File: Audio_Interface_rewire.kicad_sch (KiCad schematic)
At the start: 56 parts

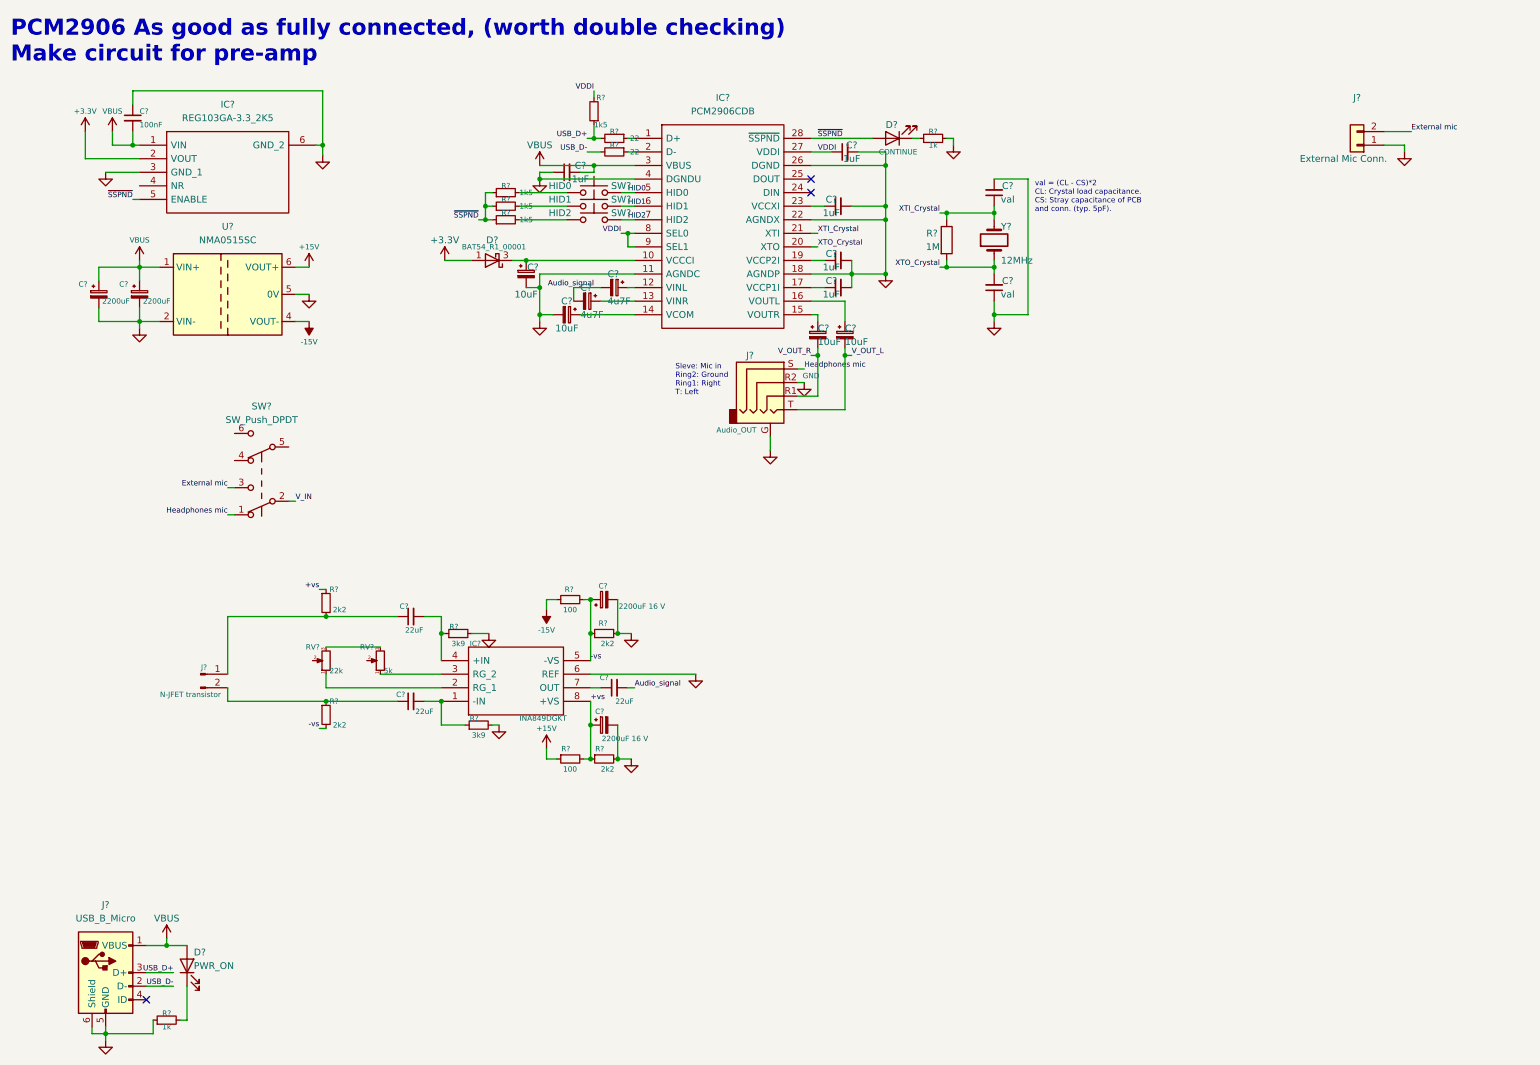
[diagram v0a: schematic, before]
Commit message: First draft of schematic completed
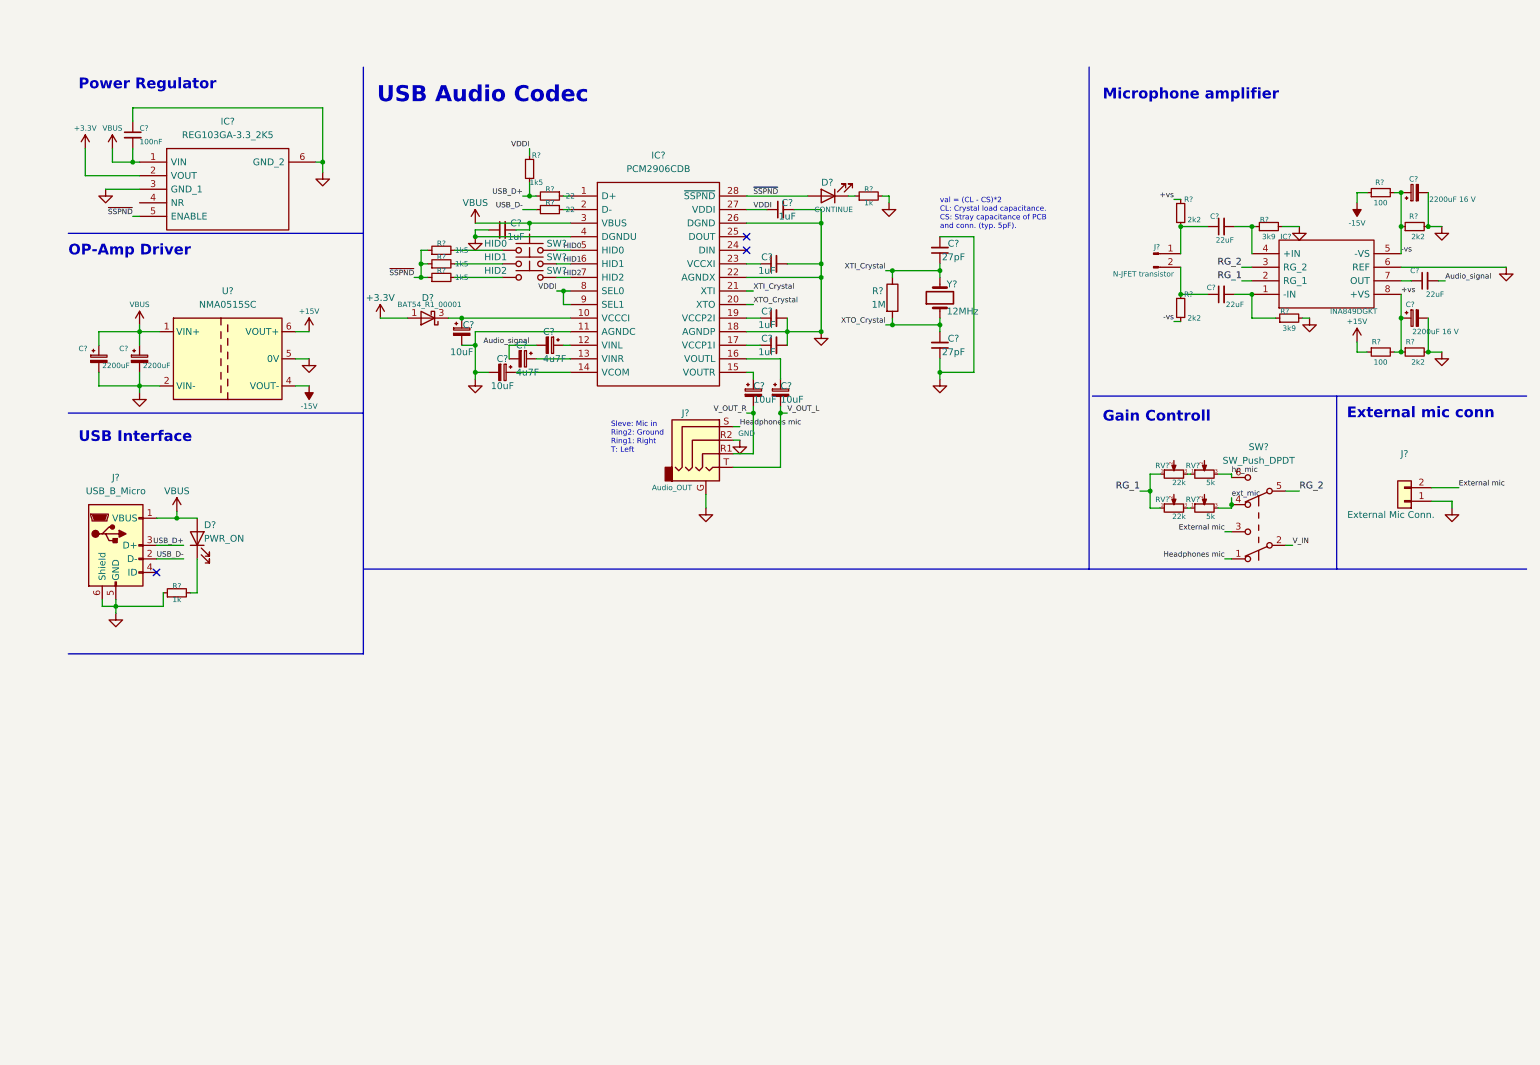
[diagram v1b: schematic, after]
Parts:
- removed RV?: 22k, symbol Device:R_Potentiometer_Small
- removed RV?: 5k, symbol Device:R_Potentiometer_Small
- added RV? (x2): 5k, symbol Device:R_Potentiometer_Small
- added RV? (x2): 22k, symbol Device:R_Potentiometer_Small
- C? (x2): value val -> 27pF
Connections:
- net ext_mic: now reaches SW?.4 (A)
- net ext_mic: now also RV?.3
- net RG_2: now reaches SW?.5 (B)
- net RG_2: now also IC?.3 (RG_2)
- net hp_mic: now reaches SW?.6 (C)
- net hp_mic: now also RV?.3
- net RG_1: now reaches IC?.2 (RG_1)
- net RG_1: now also RV?.1, RV?.1
- new net: RV?.1, RV?.3 (x2)
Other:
- note added: "External mic conn"
- note added: "Gain Controll"
- note added: "Microphone amplifier"
- note added: "OP-Amp Driver"
- note added: "Power Regulator"
- note added: "USB Audio Codec"
- note added: "USB Interface"
- note removed: "PCM2906 As good as fully connected, (worth double checking) Make circuit for pre-amp"
- moved on the sheet: C?, D?, IC?, J?, R?, SW?, U?, Y?

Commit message: Started assigning footprints for pcb, about 1/2 completed
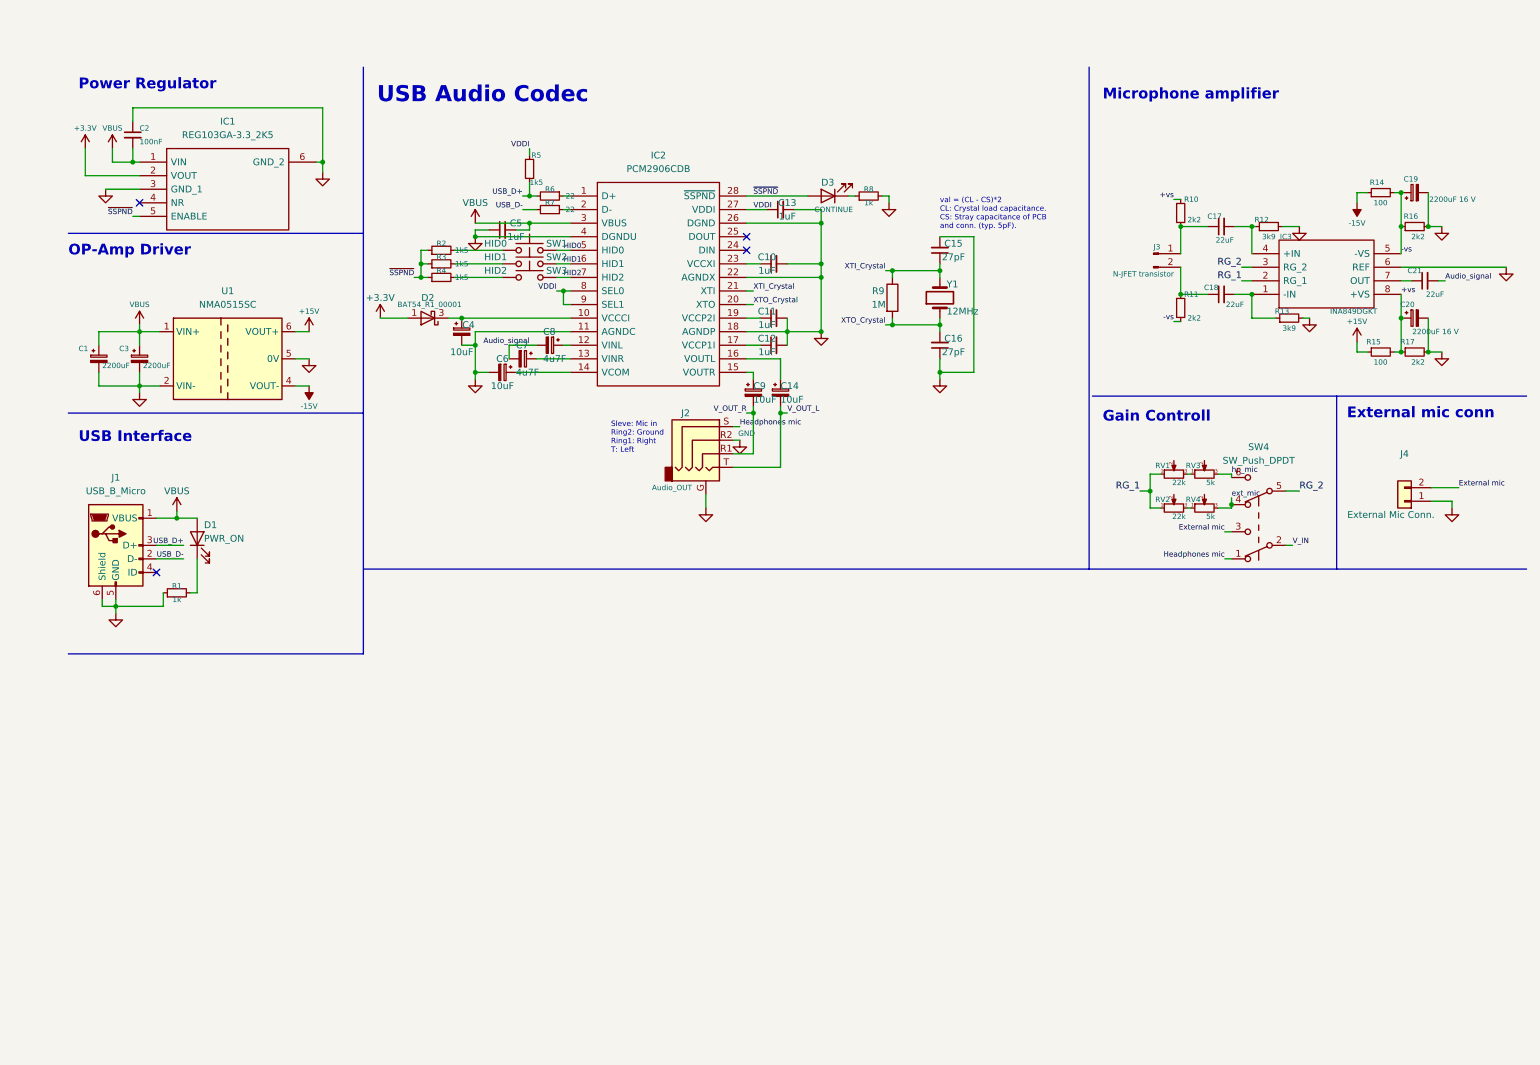
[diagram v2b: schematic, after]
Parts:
- C1, C10, C11, C12, C13, C15, C16, C2, C3, C5: renamed from C?; footprint (none) -> Capacitor_SMD:C_0805_2012Metric_Pad1.18x1.45mm_HandSolder
- C14, C17, C18, C21, C4, C6, C7, C8, C9: renamed from C?; footprint (none) -> Capacitor_THT:CP_Radial_D8.0mm_P5.00mm
- C19, C20: renamed from C?; footprint (none) -> Capacitor_THT:CP_Radial_D12.5mm_P5.00mm
- D1, D3: renamed from D?; footprint (none) -> Diode_SMD:D_0805_2012Metric_Pad1.15x1.40mm_HandSolder
- IC1: renamed from IC?; footprint SOT127P706X180-6N -> IC_Downloaded:SOT127P706X180-6N
- IC2: renamed from IC?; footprint SOP65P780X200-28N -> Package_SO:SOP65P780X200-28N
- IC3: renamed from IC?; footprint SOP65P490X110-8N -> IC_Downloaded:SOP65P490X110-8N
- J1: renamed from J?; footprint (none) -> Connector_USB:USB_B_Lumberg_2411_02_Horizontal
- J2: renamed from J?; footprint (none) -> Connector_Audio:Jack_3.5mm_CUI_SJ1-3535NG_Horizontal
- J3: renamed from J?; footprint (none) -> Package_TO_SOT_SMD:SOT-23
- J4: renamed from J?; footprint (none) -> Connector_JST:JST_XH_B2B-XH-AM_1x02_P2.50mm_Vertical
- gave numbers to parts that had none: 28
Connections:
- no-connect marks 3 -> 4

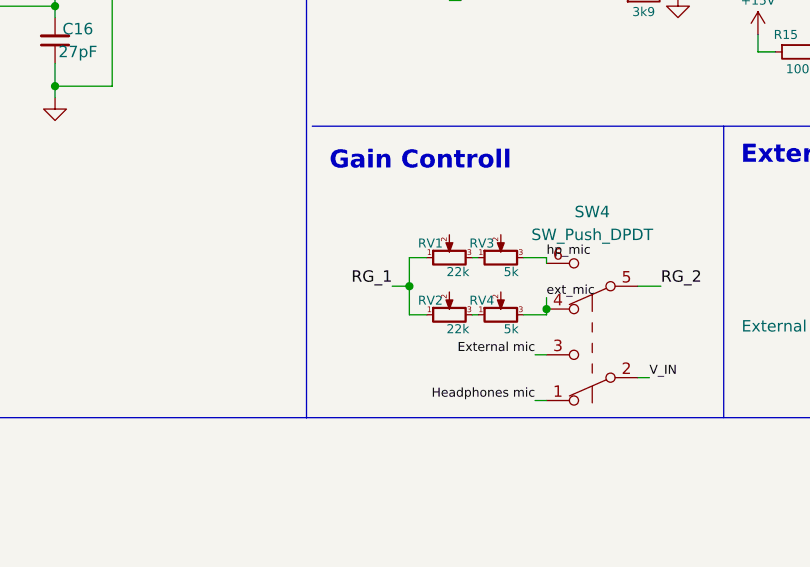
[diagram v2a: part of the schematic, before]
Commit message: Fixed gain control and added resistor footprints
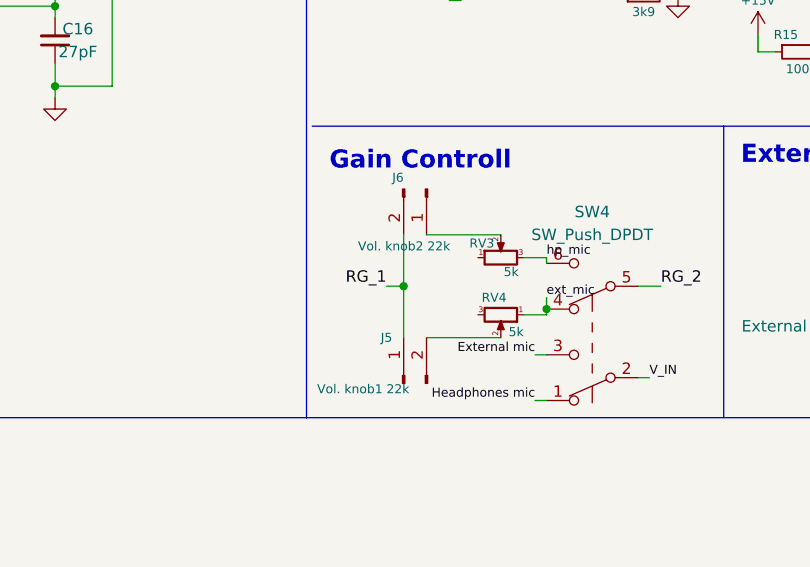
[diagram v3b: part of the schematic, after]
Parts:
- removed RV1, RV2: 22k, symbol Device:R_Potentiometer_Small
- added J5: Vol. knob1 22k, Connector_JST:JST_XH_B2B-XH-AM_1x02_P2.50mm_Vertical, symbol Connector:Conn_01x02_Male
- added J6: Vol. knob2 22k, Connector_JST:JST_XH_B2B-XH-AM_1x02_P2.50mm_Vertical, symbol Connector:Conn_01x02_Male
- R1, R10, R11, R12, R13, R14, R15, R16, R17, R2, R3, R4, R5, R6, R7, R8, R9: footprint (none) -> Resistor_SMD:R_0805_2012Metric_Pad1.20x1.40mm_HandSolder
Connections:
- net RG_1: now also J5.1 (Pin_1), J6.2 (Pin_2)
- net ext_mic: now also RV4.1; no longer RV4.3
- net at RV4.2: now also J5.2 (Pin_2)
- net at RV3.2: now also J6.1 (Pin_1)
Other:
- moved on the sheet: RV4

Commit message: Completed first draft of footprint assignment
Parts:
- RV3, RV4: footprint (none) -> IC_Downloaded:3362P_1
- SW1, SW2, SW3: footprint (none) -> Connector_JST:JST_XH_B2B-XH-AM_1x02_P2.50mm_Vertical
- SW4: footprint (none) -> Connector_JST:JST_XH_B6B-XH-AM_1x06_P2.50mm_Vertical
- Y1: footprint (none) -> IC_Downloaded:HC49US12000000ABJB
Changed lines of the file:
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@@
     (property "Reference" "SW1" (id 0) (at 103.505 45.085 0))
     (property "Value" "HID0" (id 1) (at 92.075 45.085 0))
-    (property "Footprint" "" (id 2) (at 98.425 41.275 0)
+    (property "Footprint" "Connector_JST:JST_XH_B2B-XH-AM_1x02_P2.50mm_Vertical" (id 2) (at 98.425 41.275 0)
       (effects (font (size 1.27 1.27)) hide)
     )
@@
       (effects (font (size 1 1)) (justify right))
     )
-    (property "Footprint" "" (id 2) (at 224.79 94.615 0)
+    (property "Footprint" "IC_Downloaded:3362P_1" (id 2) (at 224.79 94.615 0)
       (effects (font (size 1.27 1.27)) hide)
     )
@@
     (property "Reference" "SW4" (id 0) (at 234.95 83.185 0))
     (property "Value" "SW_Push_DPDT" (id 1) (at 234.95 85.725 0))
-    (property "Footprint" "" (id 2) (at 234.95 101.6 0)
+    (property "Footprint" "Connector_JST:JST_XH_B6B-XH-AM_1x06_P2.50mm_Vertical" (id 2) (at 234.95 101.6 0)
       (effects (font (size 1.27 1.27)) hide)
     )
@@
     (property "Reference" "SW3" (id 0) (at 103.505 50.165 0))
     (property "Value" "HID2" (id 1) (at 92.075 50.165 0))
-    (property "Footprint" "" (id 2) (at 98.425 46.355 0)
+    (property "Footprint" "Connector_JST:JST_XH_B2B-XH-AM_1x02_P2.50mm_Vertical" (id 2) (at 98.425 46.355 0)
       (effects (font (size 1.27 1.27)) hide)
     )
@@
     (property "Reference" "SW2" (id 0) (at 103.505 47.625 0))
     (property "Value" "HID1" (id 1) (at 92.075 47.625 0))
-    (property "Footprint" "" (id 2) (at 98.425 43.815 0)
+    (property "Footprint" "Connector_JST:JST_XH_B2B-XH-AM_1x02_P2.50mm_Vertical" (id 2) (at 98.425 43.815 0)
       (effects (font (size 1.27 1.27)) hide)
     )
@@
       (effects (font (size 1 1)) (justify right))
     )
-    (property "Footprint" "" (id 2) (at 224.79 88.265 0)
+    (property "Footprint" "IC_Downloaded:3362P_1" (id 2) (at 224.79 88.265 0)
       (effects (font (size 1.27 1.27)) hide)
     )
@@
       (effects (font (size 1.27 1.27)) (justify right))
     )
-    (property "Footprint" "" (id 2) (at 175.26 55.245 0)
+    (property "Footprint" "IC_Downloaded:HC49US12000000ABJB" (id 2) (at 175.26 55.245 0)
       (effects (font (size 1.27 1.27)) hide)
     )
@@
     )
     (path "/d03554fa-c78c-4476-a461-c4cfa081f890"
-      (reference "RV3") (unit 1) (value "5k") (footprint "")
+      (reference "RV3") (unit 1) (value "5k") (footprint "IC_Downloaded:3362P_1")
     )
     (path "/10c81531-80a9-47ad-a8c8-623f94beb732"
-      (reference "RV4") (unit 1) (value "5k") (footprint "")
+      (reference "RV4") (unit 1) (value "5k") (footprint "IC_Downloaded:3362P_1")
     )
     (path "/0a4ea7d6-f27d-477e-bcf8-495dd5b7aea9"
-      (reference "SW1") (unit 1) (value "HID0") (footprint "")
+      (reference "SW1") (unit 1) (value "HID0") (footprint "Connector_JST:JST_XH_B2B-XH-AM_1x02_P2.50mm_Vertical")
     )
     (path "/a1ea24c1-4b37-49ac-930c-869d66b686a0"
-      (reference "SW2") (unit 1) (value "HID1") (footprint "")
+      (reference "SW2") (unit 1) (value "HID1") (footprint "Connector_JST:JST_XH_B2B-XH-AM_1x02_P2.50mm_Vertical")
     )
     (path "/3023fa5b-054e-4618-bf6c-08db583e4d4c"
-      (reference "SW3") (unit 1) (value "HID2") (footprint "")
+      (reference "SW3") (unit 1) (value "HID2") (footprint "Connector_JST:JST_XH_B2B-XH-AM_1x02_P2.50mm_Vertical")
     )
     (path "/1d43ce9e-2ec7-48a4-aee4-30249739a3ac"
-      (reference "SW4") (unit 1) (value "SW_Push_DPDT") (footprint "")
+      (reference "SW4") (unit 1) (value "SW_Push_DPDT") (footprint "Connector_JST:JST_XH_B6B-XH-AM_1x06_P2.50mm_Vertical")
     )
     (path "/65ca9e74-0d83-46b5-87b7-a8da27f803b8"
@@
     )
     (path "/e484bef1-98be-4f65-8864-c7ee0f774192"
-      (reference "Y1") (unit 1) (value "12MHz") (footprint "")
-    )
-  )
+      (reference "Y1") (unit 1) (value "12MHz") (footprint "IC_Downloaded:HC49US12000000ABJB")
+    )
+  )

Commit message: First draft of pcb layout completed
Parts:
- removed J2: Audio_OUT, Connector_Audio:Jack_3.5mm_CUI_SJ1-3535NG_Horizontal, symbol Connector:AudioJack4_Ground
- removed J3: N-JFET transistor, Package_TO_SOT_SMD:SOT-23, symbol Connector:Conn_01x02_Male
- added H1, H2, H3, H4: M4, MountingHole:MountingHole_4.3mm_M4_Pad, symbol Mechanical:MountingHole
- added J2: SJ-435107RS, IC_Downloaded:SJ435107RS, symbol global_lib:SJ-435107RS
- added Q1: J304, Package_TO_SOT_SMD:SOT-23, symbol Transistor_FET:BF545B
- D2: footprint Package_TO_SOT_SMD:SOT-323_SC-70 -> Package_TO_SOT_SMD:SOT-323_SC-70_Handsoldering
- renumbered C11 to C10, C12 to C11, C13 to C12, C9 to C13, C10 to C9, J5 to J3, J6 to J4, J4 to J5, RV3 to RV1, RV4 to RV2
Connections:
- net GND: now also J2.4 (RING_2)
- net Headphones mic: now also J2.1 (SLEEVE)
- net V_IN: now also Q1.3 (G)
- net V_OUT_L: now also J2.2 (TIP)
- net V_OUT_R: now also J2.3 (RING_1)
- net ext_mic: now also RV2.3; no longer RV2.1
- net at C18.1, R11.1: now also Q1.1 (S)
- net at C17.1, R10.2: now also Q1.2 (D)
- no-connect marks 4 -> 8
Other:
- note added: "https://www.mouser.se/datasheet/2/670/sj_435107-1779267.pdf"
- moved on the sheet: C13, C14, RV2
